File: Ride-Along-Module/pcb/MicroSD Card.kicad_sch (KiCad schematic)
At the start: 2 parts, among them J2 Micro_SD_Card

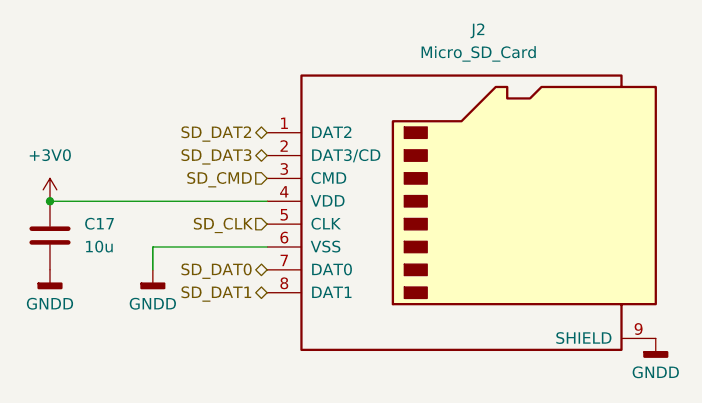
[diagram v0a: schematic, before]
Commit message: More reuse blocks. Added battery circuit to ride along board
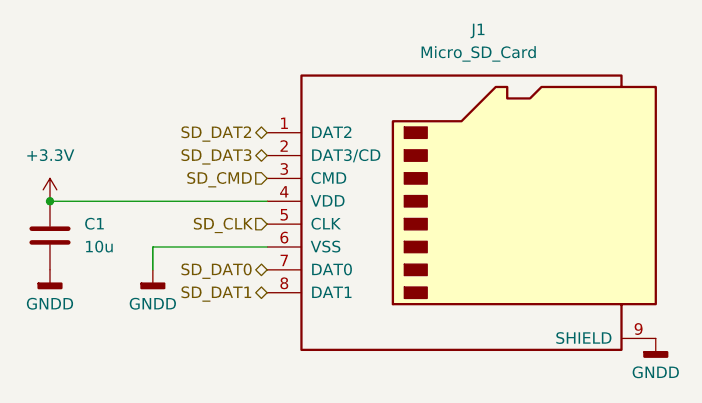
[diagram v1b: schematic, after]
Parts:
- renumbered C17 to C1, J2 to J1
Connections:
- net +3V0 renamed +3.3V
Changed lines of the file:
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@@
 		(dnp no)
 		(fields_autoplaced yes)
-		(property "Reference" "#PWR033"
+		(property "Reference" "#PWR0101"
 			(at 113.03 101.6 0)
 			(effects
@@
 			)
 			(project ""
-				(path "/ba7b4294-8d75-4b9e-892f-fb52727887ec/b45c8800-2d43-45f4-a459-8e5ce292fc5a"
-					(reference "#PWR033")
+				(path "/ba7b4294-8d75-4b9e-892f-fb52727887ec/02a5c5f6-b4e2-435d-aca7-a6d22478aa51"
+					(reference "#PWR0101")
+					(unit 1)
+				)
+			)
+		)
+	)
+	(symbol
+		(lib_id "power:+3.3V")
+		(at 101.6 87.63 0)
+		(unit 1)
+		(exclude_from_sim no)
+		(in_bom yes)
+		(on_board yes)
+		(dnp no)
+		(fields_autoplaced yes)
+		(property "Reference" "#PWR0104"
+			(at 101.6 91.44 0)
+			(effects
+				(font
+					(size 1.27 1.27)
+				)
+				(hide yes)
+			)
+		)
+		(property "Value" "+3.3V"
+			(at 101.6 82.55 0)
+			(effects
+				(font
+					(size 1.27 1.27)
+				)
+			)
+		)
+		(property "Footprint" ""
+			(at 101.6 87.63 0)
+			(effects
+				(font
+					(size 1.27 1.27)
+				)
+				(hide yes)
+			)
+		)
+		(property "Datasheet" ""
+			(at 101.6 87.63 0)
+			(effects
+				(font
+					(size 1.27 1.27)
+				)
+				(hide yes)
+			)
+		)
+		(property "Description" "Power symbol creates a global label with name \"+3.3V\""
+			(at 101.6 87.63 0)
+			(effects
+				(font
+					(size 1.27 1.27)
+				)
+				(hide yes)
+			)
+		)
+		(pin "1"
+		)
+		(instances
+			(project ""
+				(path "/7761db1c-f9c0-4350-aff2-01ef05a45511"
+					(reference "#PWR02")
+					(unit 1)
+				)
+			)
+			(project ""
+				(path "/ba7b4294-8d75-4b9e-892f-fb52727887ec/02a5c5f6-b4e2-435d-aca7-a6d22478aa51"
+					(reference "#PWR0104")
 					(unit 1)
 				)
@@
 		(dnp no)
 		(fields_autoplaced yes)
-		(property "Reference" "#PWR032"
+		(property "Reference" "#PWR0103"
 			(at 101.6 101.6 0)
 			(effects
@@
 			)
 			(project ""
-				(path "/ba7b4294-8d75-4b9e-892f-fb52727887ec/b45c8800-2d43-45f4-a459-8e5ce292fc5a"
-					(reference "#PWR032")
-					(unit 1)
-				)
-			)
-		)
-	)
-	(symbol
-		(lib_id "power:+3V0")
-		(at 101.6 87.63 0)
-		(unit 1)
-		(exclude_from_sim no)
-		(in_bom yes)
-		(on_board yes)
-		(dnp no)
-		(fields_autoplaced yes)
-		(property "Reference" "#PWR031"
-			(at 101.6 91.44 0)
-			(effects
-				(font
-					(size 1.27 1.27)
-				)
-				(hide yes)
-			)
-		)
-		(property "Value" "+3V0"
-			(at 101.6 82.55 0)
-			(effects
-				(font
-					(size 1.27 1.27)
-				)
-			)
-		)
-		(property "Footprint" ""
-			(at 101.6 87.63 0)
-			(effects
-				(font
-					(size 1.27 1.27)
-				)
-				(hide yes)
-			)
-		)
-		(property "Datasheet" ""
-			(at 101.6 87.63 0)
-			(effects
-				(font
-					(size 1.27 1.27)
-				)
-				(hide yes)
-			)
-		)
-		(property "Description" "Power symbol creates a global label with name \"+3V0\""
-			(at 101.6 87.63 0)
-			(effects
-				(font
-					(size 1.27 1.27)
-				)
-				(hide yes)
-			)
-		)
-		(pin "1"
-		)
-		(instances
-			(project ""
-				(path "/7761db1c-f9c0-4350-aff2-01ef05a45511"
-					(reference "#PWR02")
-					(unit 1)
-				)
-			)
-			(project ""
-				(path "/ba7b4294-8d75-4b9e-892f-fb52727887ec/b45c8800-2d43-45f4-a459-8e5ce292fc5a"
-					(reference "#PWR031")
+				(path "/ba7b4294-8d75-4b9e-892f-fb52727887ec/02a5c5f6-b4e2-435d-aca7-a6d22478aa51"
+					(reference "#PWR0103")
 					(unit 1)
 				)
@@
 		(dnp no)
 		(fields_autoplaced yes)
-		(property "Reference" "#PWR034"
+		(property "Reference" "#PWR0102"
 			(at 168.91 109.22 0)
 			(effects
@@
 			)
 			(project ""
-				(path "/ba7b4294-8d75-4b9e-892f-fb52727887ec/b45c8800-2d43-45f4-a459-8e5ce292fc5a"
-					(reference "#PWR034")
+				(path "/ba7b4294-8d75-4b9e-892f-fb52727887ec/02a5c5f6-b4e2-435d-aca7-a6d22478aa51"
+					(reference "#PWR0102")
 					(unit 1)
 				)
@@
 		(dnp no)
 		(fields_autoplaced yes)
-		(property "Reference" "C17"
+		(property "Reference" "C1"
 			(at 105.41 90.1699 0)
 			(effects
@@
 			)
 			(project ""
-				(path "/ba7b4294-8d75-4b9e-892f-fb52727887ec/b45c8800-2d43-45f4-a459-8e5ce292fc5a"
-					(reference "C17")
+				(path "/ba7b4294-8d75-4b9e-892f-fb52727887ec/02a5c5f6-b4e2-435d-aca7-a6d22478aa51"
+					(reference "C1")
 					(unit 1)
 				)
@@
 		(dnp no)
 		(fields_autoplaced yes)
-		(property "Reference" "J2"
+		(property "Reference" "J1"
 			(at 149.225 68.58 0)
 			(effects
@@
 			)
 			(project ""
-				(path "/ba7b4294-8d75-4b9e-892f-fb52727887ec/b45c8800-2d43-45f4-a459-8e5ce292fc5a"
-					(reference "J2")
-					(unit 1)
-				)
+				(path "/ba7b4294-8d75-4b9e-892f-fb52727887ec/02a5c5f6-b4e2-435d-aca7-a6d22478aa51"
+					(reference "J1")
+					(unit 1)
+				)

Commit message: Ride-Along Module Rev. 1
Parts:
- C15: renamed from C1; footprint Capacitor_SMD:C_0603_1608Metric_Pad1.08x0.95mm_HandSolder -> Capacitor_SMD:C_0603_1608Metric
- J2: renamed from J1; Purchase (none) -> https://www.digikey.com/en/products/detail/molex/0472192001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
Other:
- company: (none) -> Rowan Rocketry
- title: (none) -> Ride-Along Module
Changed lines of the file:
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@@
 	(generator_version "9.0")
 	(paper "A4")
+	(title_block
+		(title "Ride-Along Module")
+		(date "2025-04-10")
+		(rev "1")
+		(company "Rowan Rocketry")
+	)
 	(junction
 		(at 101.6 87.63)
@@
 		(dnp no)
 		(fields_autoplaced yes)
-		(property "Reference" "#PWR0101"
+		(property "Reference" "#PWR032"
 			(at 113.03 101.6 0)
 			(effects
@@
 			(project ""
 				(path "/ba7b4294-8d75-4b9e-892f-fb52727887ec/02a5c5f6-b4e2-435d-aca7-a6d22478aa51"
-					(reference "#PWR0101")
+					(reference "#PWR032")
 					(unit 1)
 				)
@@
 		(dnp no)
 		(fields_autoplaced yes)
-		(property "Reference" "#PWR0104"
+		(property "Reference" "#PWR030"
 			(at 101.6 91.44 0)
 			(effects
@@
 			(project ""
 				(path "/ba7b4294-8d75-4b9e-892f-fb52727887ec/02a5c5f6-b4e2-435d-aca7-a6d22478aa51"
-					(reference "#PWR0104")
+					(reference "#PWR030")
 					(unit 1)
 				)
@@
 		(dnp no)
 		(fields_autoplaced yes)
-		(property "Reference" "#PWR0103"
+		(property "Reference" "#PWR031"
 			(at 101.6 101.6 0)
 			(effects
@@
 			(project ""
 				(path "/ba7b4294-8d75-4b9e-892f-fb52727887ec/02a5c5f6-b4e2-435d-aca7-a6d22478aa51"
-					(reference "#PWR0103")
+					(reference "#PWR031")
 					(unit 1)
 				)
@@
 		(dnp no)
 		(fields_autoplaced yes)
-		(property "Reference" "#PWR0102"
+		(property "Reference" "#PWR033"
 			(at 168.91 109.22 0)
 			(effects
@@
 			(project ""
 				(path "/ba7b4294-8d75-4b9e-892f-fb52727887ec/02a5c5f6-b4e2-435d-aca7-a6d22478aa51"
-					(reference "#PWR0102")
+					(reference "#PWR033")
 					(unit 1)
 				)
@@
 		(dnp no)
 		(fields_autoplaced yes)
-		(property "Reference" "C1"
+		(property "Reference" "C15"
 			(at 105.41 90.1699 0)
 			(effects
@@
 			)
 		)
-		(property "Footprint" "Capacitor_SMD:C_0603_1608Metric_Pad1.08x0.95mm_HandSolder"
+		(property "Footprint" "Capacitor_SMD:C_0603_1608Metric"
 			(at 102.5652 95.25 0)
 			(effects
@@
 			(project ""
 				(path "/ba7b4294-8d75-4b9e-892f-fb52727887ec/02a5c5f6-b4e2-435d-aca7-a6d22478aa51"
-					(reference "C1")
+					(reference "C15")
 					(unit 1)
 				)
@@
 		(dnp no)
 		(fields_autoplaced yes)
-		(property "Reference" "J1"
+		(property "Reference" "J2"
 			(at 149.225 68.58 0)
 			(effects
@@
 			)
 		)
+		(property "Purchase" "https://www.digikey.com/en/products/detail/molex/0472192001/3044807?s=N4IgTCBcDaICwHYwEYCcBaMAGLyQF0BfIA"
+			(at 148.59 87.63 0)
+			(effects
+				(font
+					(size 1.27 1.27)
+				)
+				(hide yes)
+			)
+		)
 		(pin "8"
 		)
@@
 			(project ""
 				(path "/ba7b4294-8d75-4b9e-892f-fb52727887ec/02a5c5f6-b4e2-435d-aca7-a6d22478aa51"
-					(reference "J1")
-					(unit 1)
-				)
+					(reference "J2")
+					(unit 1)
+				)
